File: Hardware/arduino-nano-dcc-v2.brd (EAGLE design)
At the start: 58.7 x 44.5 mm, 43 parts, among them IC1 7805TV, IC3 MEGA328-P, Q2 TIP41C, X1 22-23-2031

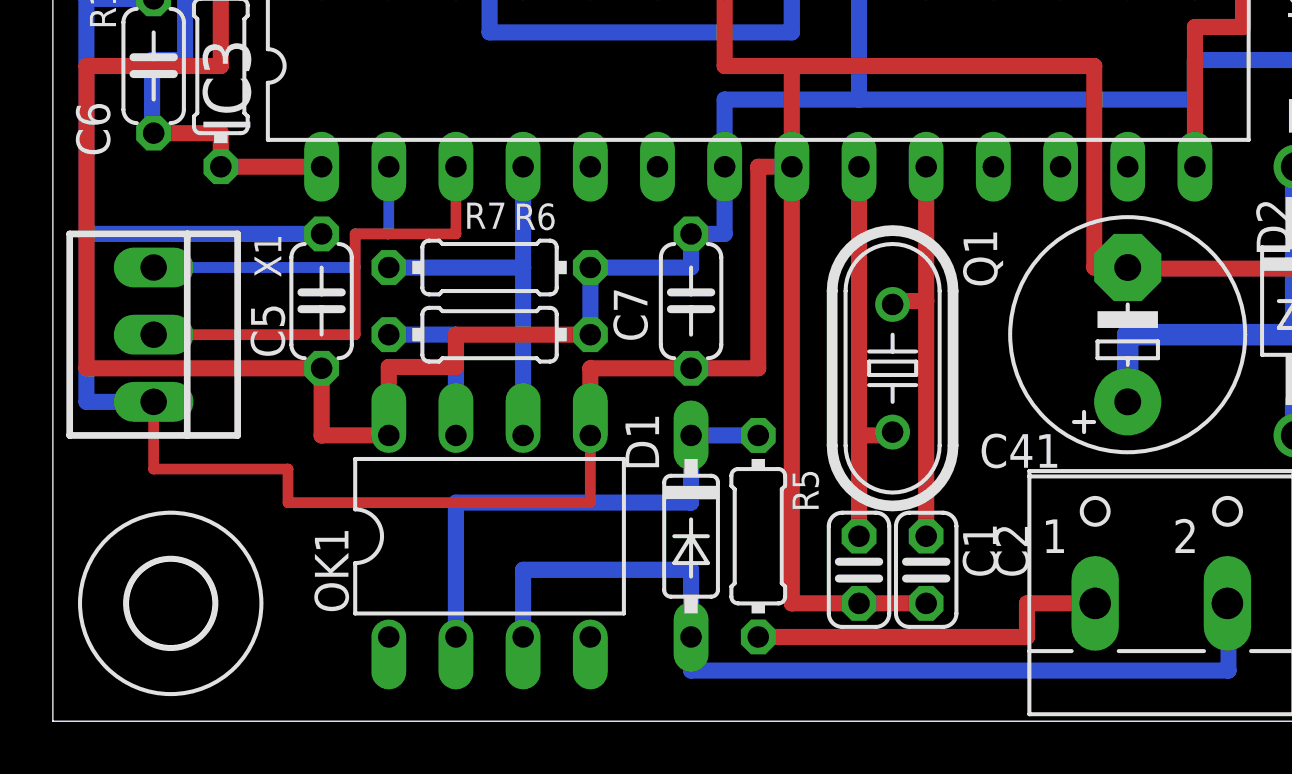
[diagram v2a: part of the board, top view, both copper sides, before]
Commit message: Added led and added zipfile for pcb production at JclPcb.
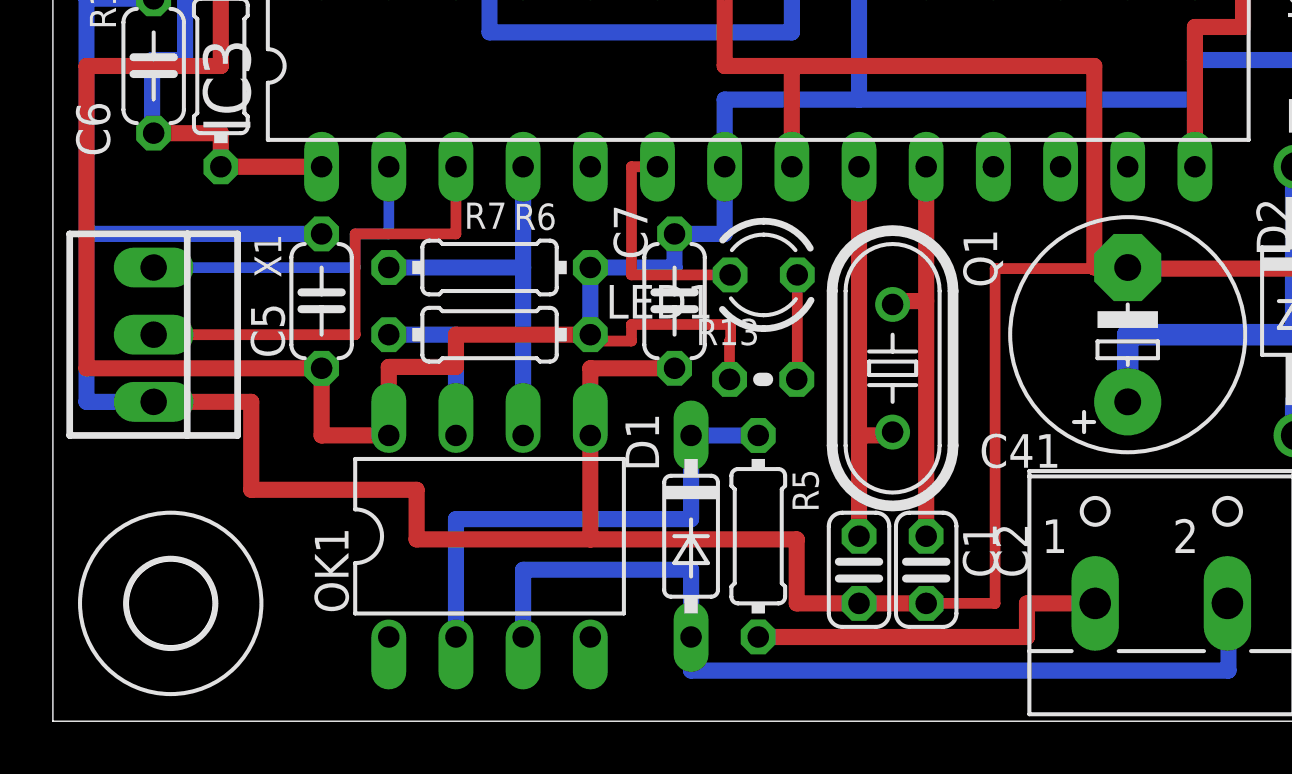
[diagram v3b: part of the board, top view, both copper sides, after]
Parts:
- added LED1: (no value), led:LED3MM
- added R13: 10k, rcl:0204V
- moved C7 0.62 mm to (23.5, 15.9)
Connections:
- new net LED: IC3.6, LED1.K
- new net N$7: LED1.A, R13.2
- net +5V: now also R13.1
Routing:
- net LED: track 0.00 -> 8.80 mm
- net +5V: track 104.2 -> 112.5 mm
- net GND: track 222.3 -> 226.9 mm
- net N$7: track 0.00 -> 3.97 mm
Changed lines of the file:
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@@
 <attribute name="VALUE" x="6.604" y="21.346" size="1.27" layer="27" ratio="10" rot="R90"/>
 </element>
-<element name="C7" library="rcl" library_urn="urn:adsk.eagle:library:334" package="C050-024X044" package3d_urn="urn:adsk.eagle:package:23643/1" value="" x="24.13" y="15.885" smashed="yes" rot="R90">
-<attribute name="NAME" x="22.479" y="14.331" size="1.27" layer="25" ratio="10" rot="R90"/>
-<attribute name="POPULARITY" value="33" x="24.13" y="15.885" size="1.778" layer="27" rot="R90" display="off"/>
-<attribute name="SPICEPREFIX" value="C" x="24.13" y="15.885" size="1.778" layer="27" rot="R90" display="off"/>
-<attribute name="VALUE" x="26.924" y="12.456" size="1.27" layer="27" ratio="10" rot="R90"/>
+<element name="C7" library="rcl" library_urn="urn:adsk.eagle:library:334" package="C050-024X044" package3d_urn="urn:adsk.eagle:package:23643/1" value="" x="23.505" y="15.885" smashed="yes" rot="R90">
+<attribute name="NAME" x="22.479" y="17.456" size="1.27" layer="25" ratio="10" rot="R90"/>
+<attribute name="POPULARITY" value="33" x="23.505" y="15.885" size="1.778" layer="27" rot="R90" display="off"/>
+<attribute name="SPICEPREFIX" value="C" x="23.505" y="15.885" size="1.778" layer="27" rot="R90" display="off"/>
+<attribute name="VALUE" x="26.299" y="12.456" size="1.27" layer="27" ratio="10" rot="R90"/>
 </element>
 <element name="X1" library="con-molex" library_urn="urn:adsk.eagle:library:165" package="22-23-2031" package3d_urn="urn:adsk.eagle:package:8078634/1" value="22-23-2031" x="3.81" y="14.615" smashed="yes" rot="R270">
@@
 <attribute name="NAME" x="11.0954" y="35.08" size="0.9906" layer="25" ratio="10" rot="R270"/>
 <attribute name="VALUE" x="8.6924" y="41.6656" size="0.9906" layer="27" ratio="10" rot="R270"/>
+</element>
+<element name="LED1" library="led" library_urn="urn:adsk.eagle:library:259" package="LED3MM" package3d_urn="urn:adsk.eagle:package:15797/1" value="" x="26.875" y="16.875" smashed="yes" rot="R180">
+<attribute name="NAME" x="24.97" y="16.494" size="1.27" layer="25" ratio="10" rot="R180"/>
+<attribute name="POPULARITY" value="97" x="26.875" y="16.875" size="1.778" layer="27" rot="R180" display="off"/>
+<attribute name="VALUE" x="24.97" y="18.526" size="1.27" layer="27" ratio="10" rot="R180"/>
+</element>
+<element name="R13" library="rcl" package="0204V" value="10k" x="26.855" y="12.925" smashed="yes">
+<attribute name="NAME" x="24.315" y="14.2204" size="0.9906" layer="25" ratio="10"/>
+<attribute name="VALUE" x="25.2294" y="12.4424" size="0.9906" layer="27" ratio="10"/>
 </element>
 </elements>
@@
 <contactref element="Q2" pad="B"/>
 <wire x1="20.32" y1="14.615" x2="20.32" y2="17.155" width="0.6096" layer="16"/>
-<wire x1="20.32" y1="17.155" x2="24.13" y2="17.155" width="0.6096" layer="16"/>
-<wire x1="24.13" y1="17.155" x2="24.13" y2="18.425" width="0.6096" layer="16"/>
-<wire x1="24.13" y1="18.425" x2="25.4" y2="18.425" width="0.6096" layer="16"/>
+<wire x1="20.32" y1="17.155" x2="23.505" y2="17.155" width="0.6096" layer="16"/>
+<wire x1="23.505" y1="17.155" x2="23.505" y2="18.425" width="0.6096" layer="16"/>
+<wire x1="23.505" y1="18.425" x2="25.4" y2="18.425" width="0.6096" layer="16"/>
 <wire x1="25.4" y1="18.425" x2="25.4" y2="20.965" width="0.6096" layer="16"/>
 <wire x1="12.7" y1="10.805" x2="10.16" y2="10.805" width="0.6096" layer="1"/>
@@
 <wire x1="54.61" y1="30.625" x2="54.61" y2="33.04" width="0.6096" layer="16"/>
 <wire x1="49.375" y1="30.625" x2="54.61" y2="30.625" width="0.6096" layer="16"/>
+<contactref element="R13" pad="1"/>
+<wire x1="25.585" y1="12.925" x2="25.585" y2="14.375" width="0.4064" layer="1"/>
+<wire x1="25.585" y1="14.375" x2="25.625" y2="14.375" width="0.4064" layer="1"/>
+<wire x1="25.625" y1="14.375" x2="25.625" y2="15" width="0.4064" layer="1"/>
+<wire x1="25.625" y1="15" x2="21.875" y2="15" width="0.4064" layer="1"/>
+<wire x1="21.875" y1="15" x2="21.875" y2="14.375" width="0.4064" layer="1"/>
+<wire x1="21.875" y1="14.375" x2="20.32" y2="14.375" width="0.4064" layer="1"/>
+<wire x1="20.32" y1="14.375" x2="20.32" y2="14.615" width="0.4064" layer="1"/>
 </signal>
 <signal name="GND">
@@
 <wire x1="27.195" y1="41.285" x2="22.115" y2="41.285" width="0.8128" layer="1"/>
 <wire x1="30.48" y1="4.455" x2="33.02" y2="4.455" width="0.6096" layer="1"/>
-<wire x1="30.48" y1="4.455" x2="27.94" y2="4.455" width="0.6096" layer="1"/>
-<wire x1="27.94" y1="4.455" x2="27.94" y2="20.965" width="0.6096" layer="1"/>
 <contactref element="X2" pad="2"/>
 <wire x1="52.07" y1="20.965" x2="53.965" y2="20.965" width="1.016" layer="16"/>
 <wire x1="53.965" y1="20.965" x2="53.965" y2="17.115" width="1.016" layer="16"/>
 <wire x1="20.32" y1="10.805" x2="20.32" y2="13.345" width="0.6096" layer="1"/>
-<wire x1="20.32" y1="13.345" x2="24.13" y2="13.345" width="0.6096" layer="1"/>
+<wire x1="20.32" y1="13.345" x2="23.505" y2="13.345" width="0.6096" layer="1"/>
 <wire x1="25.4" y1="28.585" x2="25.4" y2="24.775" width="0.6096" layer="1"/>
 <wire x1="25.4" y1="24.775" x2="27.94" y2="24.775" width="0.6096" layer="1"/>
 <wire x1="27.94" y1="24.775" x2="27.94" y2="20.965" width="0.6096" layer="1"/>
-<wire x1="24.13" y1="13.345" x2="26.67" y2="13.345" width="0.6096" layer="1"/>
-<wire x1="26.67" y1="13.345" x2="26.67" y2="20.965" width="0.6096" layer="1"/>
-<wire x1="26.67" y1="20.965" x2="27.94" y2="20.965" width="0.6096" layer="1"/>
 <wire x1="22.86" y1="31.125" x2="24.13" y2="31.125" width="0.6096" layer="1"/>
 <wire x1="24.13" y1="31.125" x2="24.13" y2="28.585" width="0.6096" layer="1"/>
 <wire x1="24.13" y1="28.585" x2="25.4" y2="28.585" width="0.6096" layer="1"/>
-<wire x1="3.81" y1="12.075" x2="3.81" y2="9.535" width="0.4064" layer="1"/>
-<wire x1="3.81" y1="9.535" x2="8.89" y2="9.535" width="0.4064" layer="1"/>
-<wire x1="8.89" y1="9.535" x2="8.89" y2="8.265" width="0.4064" layer="1"/>
-<wire x1="8.89" y1="8.265" x2="20.32" y2="8.265" width="0.4064" layer="1"/>
-<wire x1="20.32" y1="8.265" x2="20.32" y2="10.805" width="0.4064" layer="1"/>
 <wire x1="10.16" y1="18.425" x2="1.27" y2="18.425" width="0.6096" layer="16"/>
 <wire x1="1.27" y1="18.425" x2="1.27" y2="12.075" width="0.6096" layer="16"/>
@@
 <wire x1="53.965" y1="17.115" x2="40.64" y2="17.115" width="0.6096" layer="1"/>
 <wire x1="40.64" y1="17.115" x2="40.64" y2="17.155" width="0.6096" layer="1"/>
+<wire x1="33.02" y1="4.455" x2="35.625" y2="4.455" width="0.4064" layer="1"/>
+<wire x1="35.625" y1="17.115" x2="40.64" y2="17.115" width="0.4064" layer="1"/>
+<wire x1="35.625" y1="4.455" x2="35.625" y2="17.115" width="0.4064" layer="1"/>
+<wire x1="30.48" y1="4.455" x2="28.125" y2="4.455" width="0.6096" layer="1"/>
+<wire x1="28.125" y1="4.455" x2="28.125" y2="6.875" width="0.6096" layer="1"/>
+<wire x1="20.32" y1="10.805" x2="20.32" y2="6.875" width="0.6096" layer="1"/>
+<wire x1="28.125" y1="6.875" x2="20.32" y2="6.875" width="0.6096" layer="1"/>
+<wire x1="20.32" y1="6.875" x2="13.75" y2="6.875" width="0.6096" layer="1"/>
+<wire x1="13.75" y1="6.875" x2="13.75" y2="8.75" width="0.6096" layer="1"/>
+<wire x1="7.5" y1="12.075" x2="3.81" y2="12.075" width="0.6096" layer="1"/>
+<wire x1="13.75" y1="8.75" x2="7.5" y2="8.75" width="0.6096" layer="1"/>
+<wire x1="7.5" y1="8.75" x2="7.5" y2="12.075" width="0.6096" layer="1"/>
 </signal>
 <signal name="N$17">
@@
 <contactref element="OK1" pad="2"/>
 <contactref element="D1" pad="C"/>
-<wire x1="15.24" y1="3.185" x2="15.24" y2="8.265" width="0.6096" layer="16"/>
-<wire x1="15.24" y1="8.265" x2="24.13" y2="8.265" width="0.6096" layer="16"/>
-<wire x1="24.13" y1="8.265" x2="24.13" y2="10.805" width="0.6096" layer="16"/>
+<wire x1="15.24" y1="3.185" x2="15.24" y2="7.64" width="0.6096" layer="16"/>
+<wire x1="15.24" y1="7.64" x2="24.13" y2="7.64" width="0.6096" layer="16"/>
+<wire x1="24.13" y1="7.64" x2="24.13" y2="10.805" width="0.6096" layer="16"/>
 <wire x1="24.13" y1="10.805" x2="26.67" y2="10.805" width="0.6096" layer="16"/>
 </signal>
@@
 <wire x1="11.875" y1="37.48" x2="11.875" y2="36.21" width="0.6096" layer="16"/>
 </signal>
+<signal name="LED">
+<contactref element="LED1" pad="K"/>
+<contactref element="IC3" pad="6"/>
+<wire x1="25.605" y1="16.875" x2="21.875" y2="16.875" width="0.4064" layer="1"/>
+<wire x1="21.875" y1="20.965" x2="22.86" y2="20.965" width="0.4064" layer="1"/>
+<wire x1="21.875" y1="16.875" x2="21.875" y2="20.965" width="0.4064" layer="1"/>
+</signal>
+<signal name="N$7">
+<contactref element="LED1" pad="A"/>
+<contactref element="R13" pad="2"/>
+<wire x1="28.145" y1="16.875" x2="28.145" y2="12.925" width="0.4064" layer="1"/>
+<wire x1="28.145" y1="12.925" x2="28.125" y2="12.925" width="0.4064" layer="1"/>
+</signal>
 </signals>

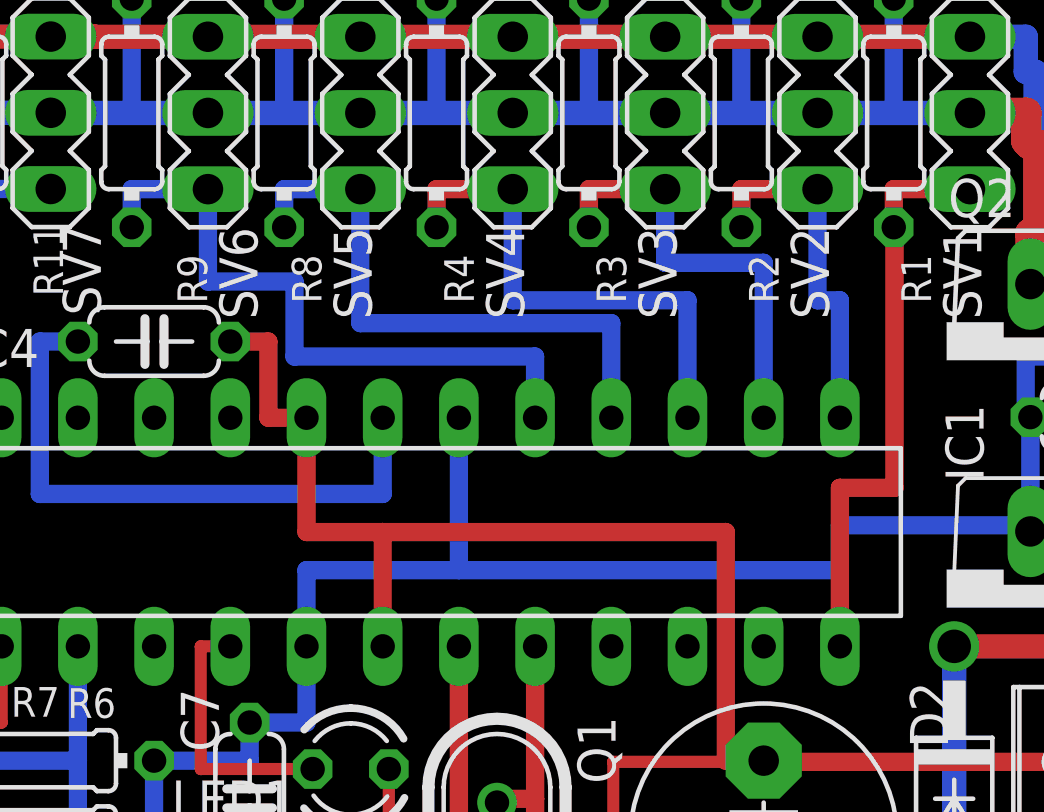
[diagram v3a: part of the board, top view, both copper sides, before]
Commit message: * Pin PB5 does not work, so moved to PC0.  * Run led added.
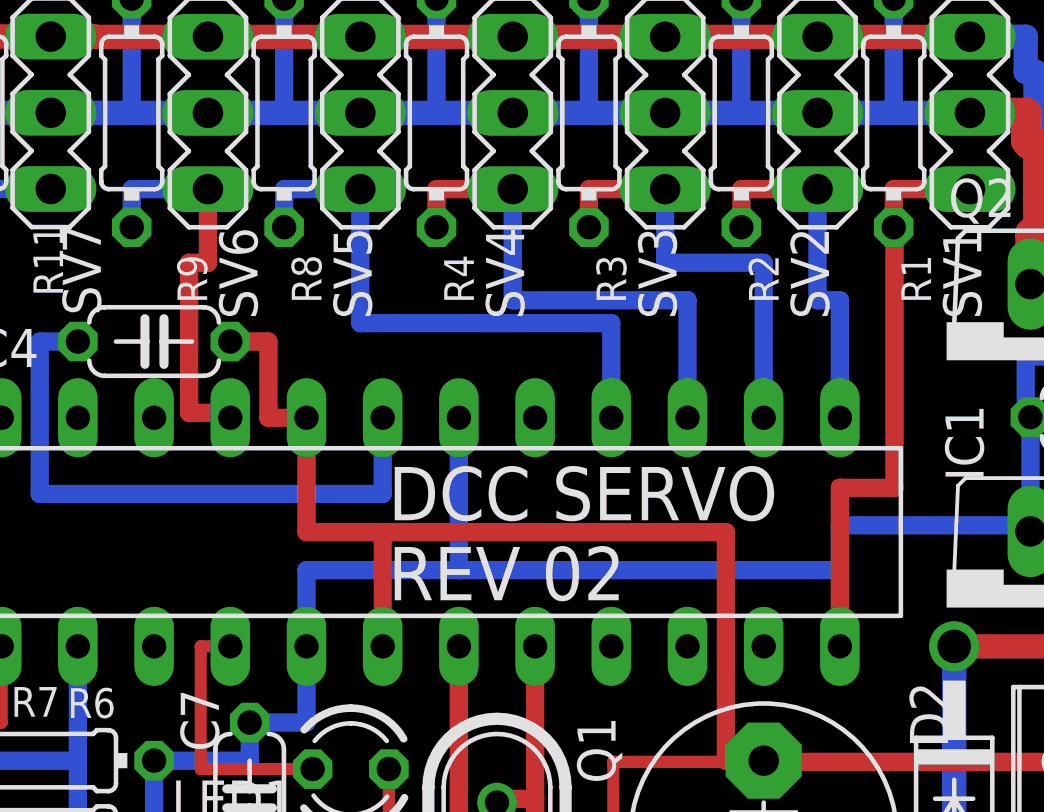
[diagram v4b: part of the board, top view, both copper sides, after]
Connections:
- net SERVO6: now also IC3.23; no longer IC3.19
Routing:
- net SERVO6: track 22.3 -> 13.4 mm
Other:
- board text added: "DCC SERVO REV 02"
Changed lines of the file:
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@@
 <wire x1="58.715" y1="44.46" x2="0" y2="44.46" width="0" layer="20"/>
 <wire x1="0" y1="44.46" x2="0" y2="0" width="0" layer="20"/>
+<text x="28.125" y="22.5" size="1.778" layer="25">DCC SERVO
+REV 02</text>
 </plain>
 <attributes>
@@
 <contactref element="R9" pad="1"/>
 <contactref element="SV6" pad="3"/>
-<contactref element="IC3" pad="19"/>
 <wire x1="19.575" y1="34.935" x2="19.575" y2="36.205" width="0.6096" layer="16"/>
 <wire x1="19.575" y1="36.205" x2="22.115" y2="36.205" width="0.6096" layer="16"/>
-<wire x1="33.02" y1="28.585" x2="33.02" y2="30.625" width="0.6096" layer="16"/>
-<wire x1="25" y1="30.625" x2="25" y2="33.125" width="0.6096" layer="16"/>
-<wire x1="22.115" y1="33.125" x2="22.115" y2="36.205" width="0.6096" layer="16"/>
-<wire x1="33.02" y1="30.625" x2="25" y2="30.625" width="0.6096" layer="16"/>
-<wire x1="25" y1="33.125" x2="22.115" y2="33.125" width="0.6096" layer="16"/>
+<contactref element="IC3" pad="23"/>
+<wire x1="22.86" y1="28.585" x2="22.86" y2="28.75" width="0.6096" layer="1"/>
+<wire x1="22.86" y1="28.75" x2="21.4884" y2="28.75" width="0.6096" layer="1"/>
+<wire x1="22.115" y1="33.75" x2="22.115" y2="36.205" width="0.6096" layer="1"/>
+<wire x1="21.4884" y1="28.75" x2="21.4884" y2="33.75" width="0.6096" layer="1"/>
+<wire x1="21.4884" y1="33.75" x2="22.115" y2="33.75" width="0.6096" layer="1"/>
 </signal>
 <signal name="N$3">
@@
 </drawing>
 <compatibility>
+<note version="6.3" minversion="6.2.2" severity="warning">
+Since Version 6.2.2 text objects can contain more than one line,
+which will not be processed correctly with this version.
+</note>
 <note version="8.2" severity="warning">
 Since Version 8.2, EAGLE supports online libraries. The ids
